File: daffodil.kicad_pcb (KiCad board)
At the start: 2 copper layers, 70.7 x 53.3 mm, 8 parts, among them J1 NEIGHBOR1, J2 NEIGHBOR2, J7 BONUS_ROW, P1 GREATFET-PROTO-AREA

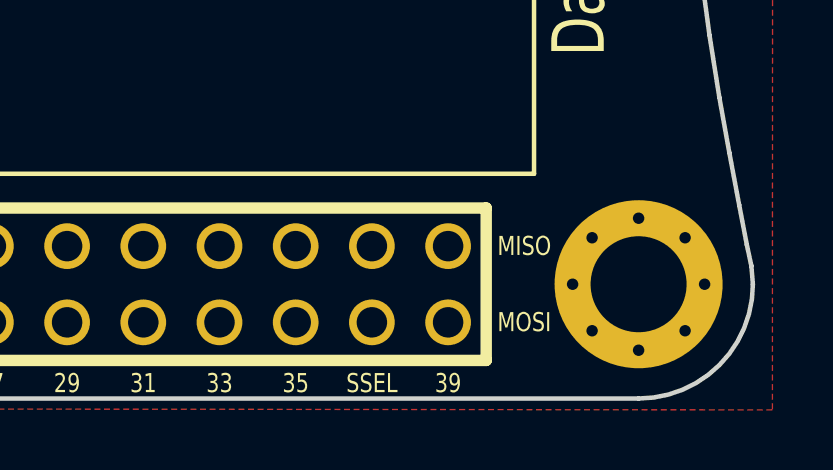
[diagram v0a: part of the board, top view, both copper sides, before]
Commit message: adopt OSHWA convention for SPI signal names https://www.oshwa.org/a-resolution-to-redefine-spi-signal-names
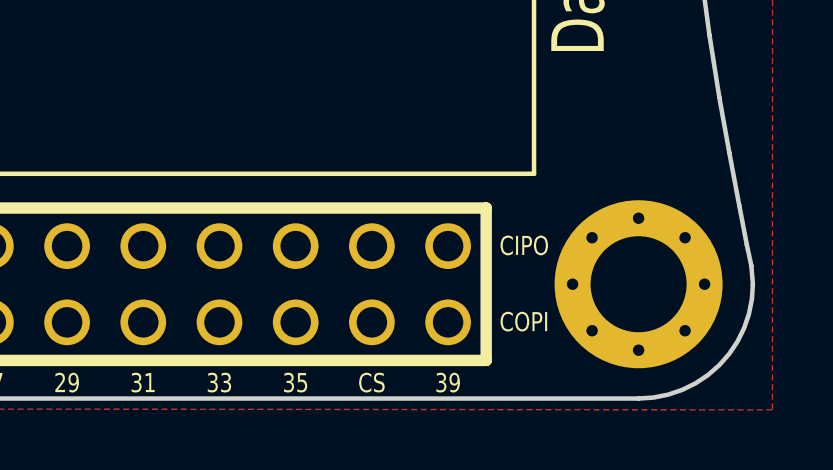
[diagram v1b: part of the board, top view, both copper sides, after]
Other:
- board text added: "CIPO"
- board text added: "COPI"
- board text added: "CS"
- board text removed: "MISO"
- board text removed: "MOSI"
- board text removed: "SSEL"
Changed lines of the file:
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@@
     (effects (font (size 0.635 0.508) (thickness 0.1016)))
   )
-  (gr_text SSEL (at 167.64 121.412) (layer F.SilkS)
+  (gr_text CS (at 167.64 121.412) (layer F.SilkS)
     (effects (font (size 0.635 0.508) (thickness 0.1016)))
   )
-  (gr_text MISO (at 172.72 116.84) (layer F.SilkS)
+  (gr_text CIPO (at 172.72 116.84) (layer F.SilkS)
     (effects (font (size 0.635 0.508) (thickness 0.1016)))
   )
-  (gr_text MOSI (at 172.72 119.38) (layer F.SilkS)
+  (gr_text COPI (at 172.72 119.38) (layer F.SilkS)
     (effects (font (size 0.635 0.508) (thickness 0.1016)))
   )
